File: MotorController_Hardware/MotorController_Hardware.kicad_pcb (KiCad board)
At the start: 2 copper layers, 124.5 x 150.9 mm, 246 parts, among them Q12 FQP30N06L, Q13 FQP30N06L, Q14 FQP30N06L, Q15 FQP30N06L, Q16 FQP30N06L, Q17 FQP30N06L, Q4 FQP30N06L, Q5 FQP30N06L, Q6 FQP30N06L, Q7 FQP30N06L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

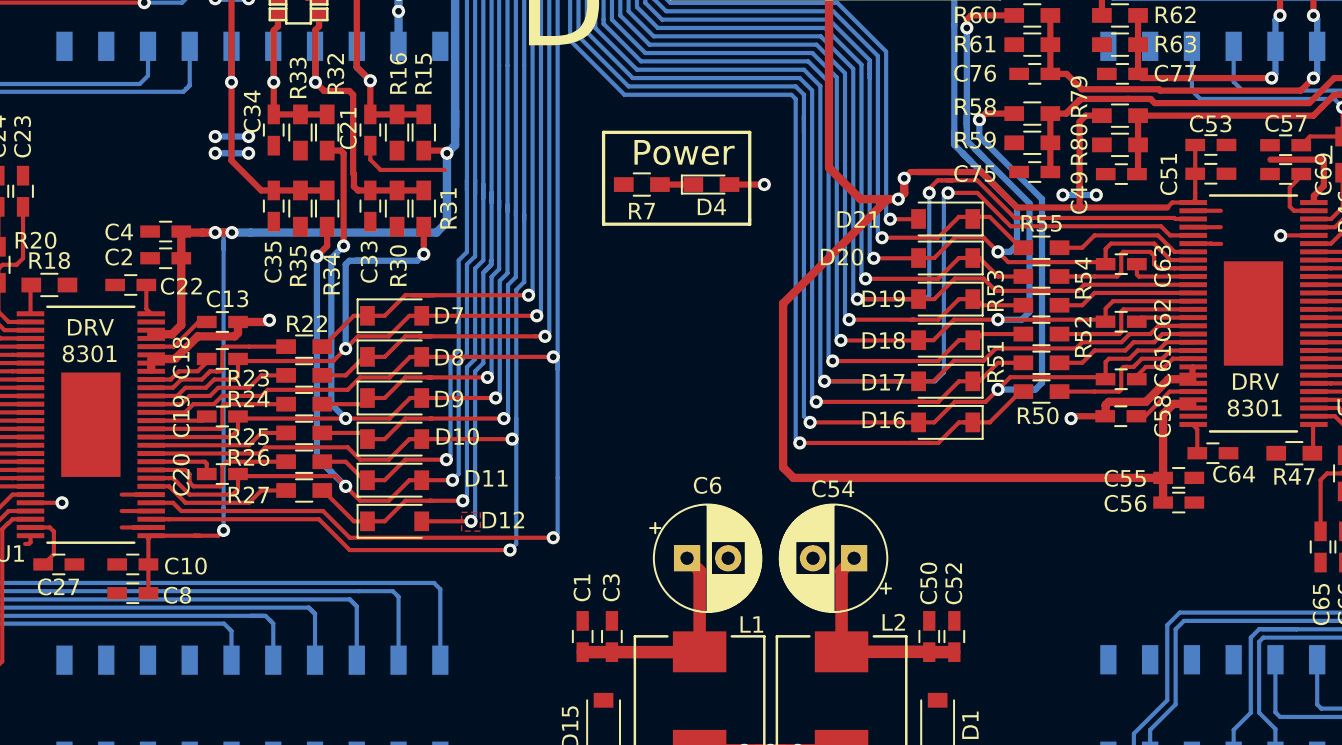
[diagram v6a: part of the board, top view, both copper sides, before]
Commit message: Created BOM
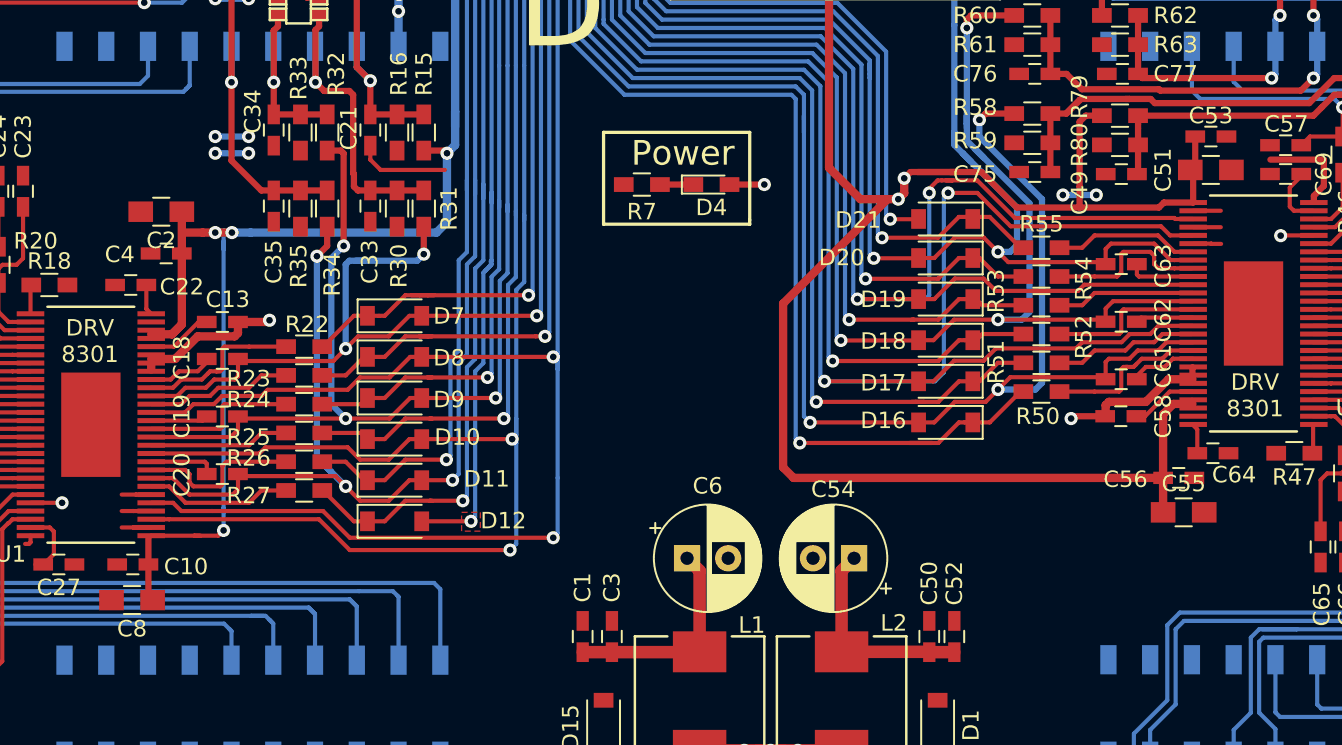
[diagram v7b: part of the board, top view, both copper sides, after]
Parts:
- C2, C51, C55, C8: footprint Capacitors_SMD:C_0603_HandSoldering -> Capacitors_SMD:C_0805_HandSoldering
- moved C2 2.85 mm to (88.2, 50.3)
- moved C55 2.12 mm to (150.3, 68.6)
- moved C56 1.50 mm to (150.0, 66.5)
- moved C4 1.33 mm to (88.5, 52.8)
- moved C53 0.51 mm to (152.0, 45.7)
- moved C8 0.42 mm to (86.4, 73.9)
- moved C51 0.23 mm to (152.0, 47.8)
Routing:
- net PVDD_M1: track 122.5 -> 126.5 mm
- net PVDD_M2: track 160.6 -> 157.7 mm

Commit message: PRR
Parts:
- moved C36 0.51 mm to (69.1, 2.97)
- moved C9 0.25 mm to (57.1, 2.97)
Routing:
- net UART_TX: track 120.2 -> 181.6 mm
- net UART_RX: track 123.5 -> 151.9 mm
- net PVDD_M1: track 126.5 -> 130.3 mm
- net MGH_B_M1: track 99.2 -> 102.6 mm
- net PVDD_M2: track 157.7 -> 161.0 mm, vias 4 -> 2
- net MGH_A_M1: track 121.2 -> 124.3 mm
- net MGL_B_M1: track 113.9 -> 117.0 mm
- net Net-(D37-Pad1): track 2.03 -> 4.15 mm
- net Net-(D3-Pad1): track 2.03 -> 4.15 mm
- net (no net): track 2.03 -> 0.00 mm, vias 2 -> 0
- net GND: track 222.6 -> 224.2 mm, vias 19 -> 21
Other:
- board text removed: "G"
